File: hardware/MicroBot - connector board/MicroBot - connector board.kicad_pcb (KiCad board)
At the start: 2 copper layers, 88.9 x 76.8 mm, 36 parts, among them J0 SMM_Mega_Shield_Connector, J1 X_Axis_Stepper_Controller, J2 Y_Axis_Stepper_Controller, J3 gen4-IB, J4 24VDC, M1 Motor_DC, U1 L9110_H-Bridge, U2 R-78C12-1.0, U3 R-78C12-1.0, U5 OKI-78SR-5_1.5-W36-C

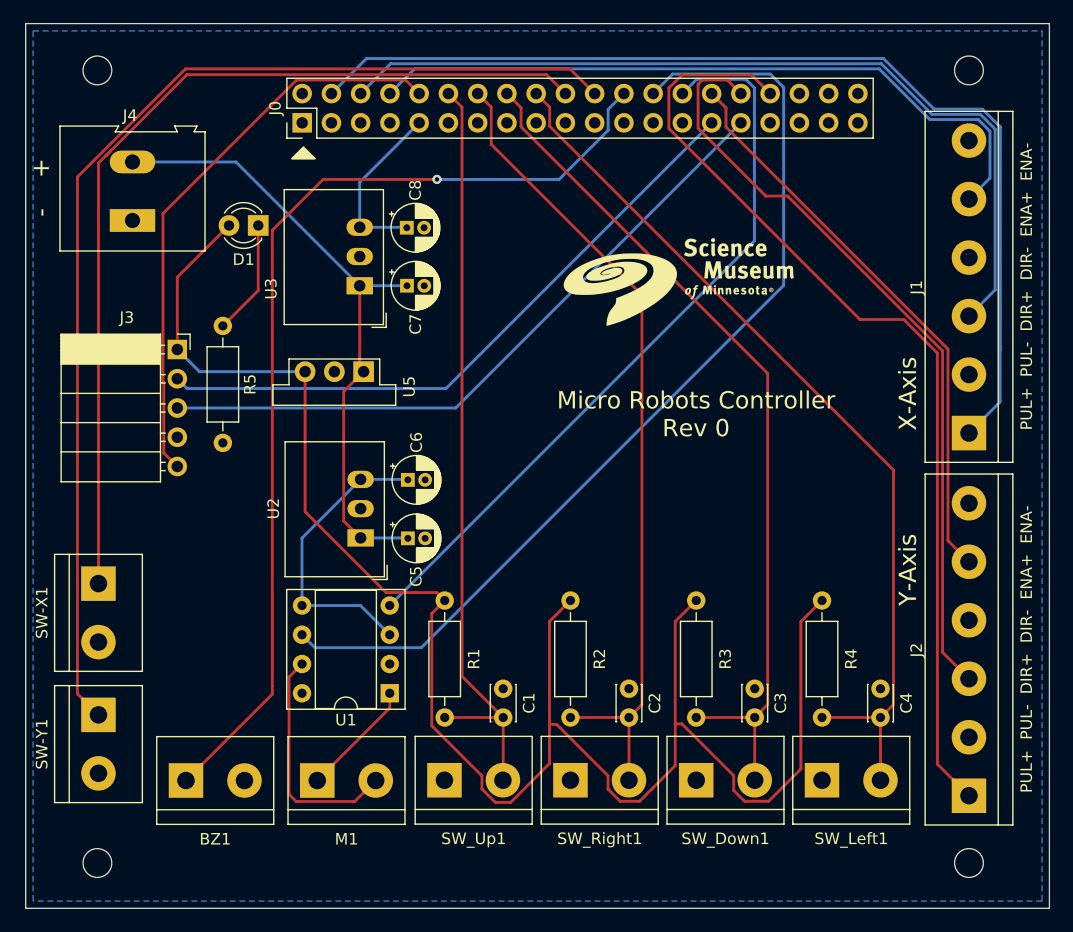
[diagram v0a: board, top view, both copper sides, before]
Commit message: fix error in PCB layout
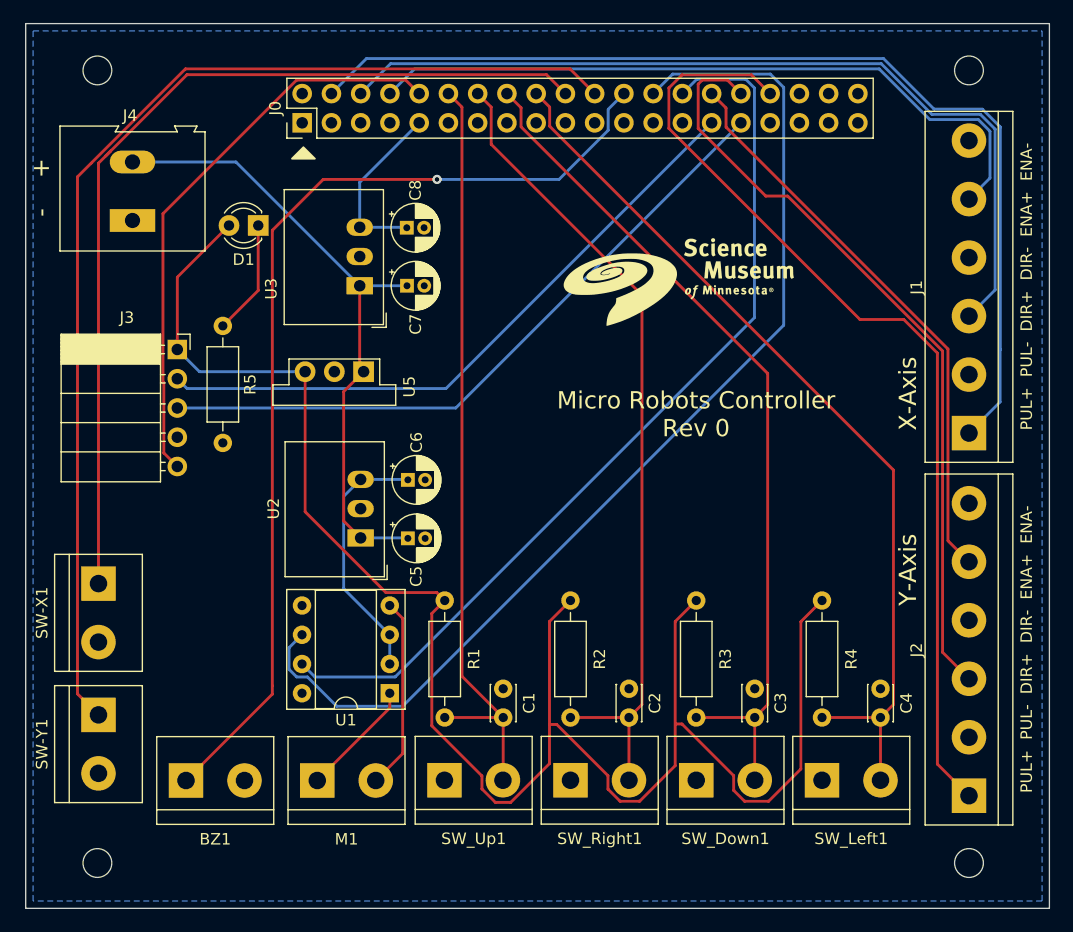
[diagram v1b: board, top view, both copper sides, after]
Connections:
- U1 pad 2: GND -> Net-(C6-Pad1)
- U1 pad 4: /MotorB -> Net-(M1-Pad2)
- U1 pad 5: Net-(C6-Pad1) -> GND
- U1 pad 7: Net-(M1-Pad2) -> /MotorB
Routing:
- net /MotorB: track 65.1 -> 79.7 mm
- net /MotorA: track 85.0 -> 94.6 mm
- net Net-(M1-Pad2): track 20.3 -> 16.6 mm
- net Net-(C6-Pad1): track 25.9 -> 22.4 mm
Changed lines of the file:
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@@
       (net 42 "Net-(M1-Pad1)") (pinfunction "OA") (pintype "output"))
     (pad "2" thru_hole oval (at 0 2.54 180) (size 1.6 1.6) (drill 0.8) (layers *.Cu *.Mask)
-      (net 2 "GND") (pinfunction "GND") (pintype "power_in"))
+      (net 3 "Net-(C6-Pad1)") (pinfunction "VCC") (pintype "power_in"))
     (pad "3" thru_hole oval (at 0 5.08 180) (size 1.6 1.6) (drill 0.8) (layers *.Cu *.Mask)
       (net 3 "Net-(C6-Pad1)") (pinfunction "VCC") (pintype "power_in"))
     (pad "4" thru_hole oval (at 0 7.62 180) (size 1.6 1.6) (drill 0.8) (layers *.Cu *.Mask)
-      (net 28 "/MotorB") (pinfunction "IB") (pintype "input"))
+      (net 43 "Net-(M1-Pad2)") (pinfunction "OB") (pintype "output"))
     (pad "5" thru_hole oval (at 7.62 7.62 180) (size 1.6 1.6) (drill 0.8) (layers *.Cu *.Mask)
-      (net 3 "Net-(C6-Pad1)") (pinfunction "VCC") (pintype "power_in"))
+      (net 2 "GND") (pinfunction "GND") (pintype "power_in"))
     (pad "6" thru_hole oval (at 7.62 5.08 180) (size 1.6 1.6) (drill 0.8) (layers *.Cu *.Mask)
       (net 26 "/MotorA") (pinfunction "IA") (pintype "input"))
     (pad "7" thru_hole oval (at 7.62 2.54 180) (size 1.6 1.6) (drill 0.8) (layers *.Cu *.Mask)
-      (net 43 "Net-(M1-Pad2)") (pinfunction "OB") (pintype "output"))
+      (net 28 "/MotorB") (pinfunction "IB") (pintype "input"))
     (pad "8" thru_hole oval (at 7.62 0 180) (size 1.6 1.6) (drill 0.8) (layers *.Cu *.Mask)
       (net 2 "GND") (pinfunction "GND") (pintype "power_in"))
@@
   (segment (start 147.5655 71.1345) (end 143.3 75.4) (width 0.25) (layer "B.Cu") (net 1))
   (segment (start 143.3 75.4) (end 132.7 75.4) (width 0.25) (layer "B.Cu") (net 1))
-  (segment (start 120.975989 106.542088) (end 120.975989 112.403489) (width 0.25) (layer "B.Cu") (net 3))
-  (segment (start 126.055989 112.403489) (end 128.595989 114.943489) (width 0.25) (layer "B.Cu") (net 3))
+  (segment (start 124.591478 110.938978) (end 128.595989 114.943489) (width 0.25) (layer "B.Cu") (net 3))
+  (segment (start 126.065989 101.452088) (end 124.591478 102.926599) (width 0.25) (layer "B.Cu") (net 3))
+  (segment (start 124.591478 102.926599) (end 124.591478 110.938978) (width 0.25) (layer "B.Cu") (net 3))
   (segment (start 130.129989 101.452088) (end 130.16939 101.491489) (width 0.25) (layer "B.Cu") (net 3))
-  (segment (start 120.975989 112.403489) (end 126.055989 112.403489) (width 0.25) (layer "B.Cu") (net 3))
+  (segment (start 128.595989 114.943489) (end 128.595989 117.483489) (width 0.25) (layer "B.Cu") (net 3))
   (segment (start 126.065989 101.452088) (end 130.129989 101.452088) (width 0.25) (layer "B.Cu") (net 3))
-  (segment (start 126.065989 101.452088) (end 120.975989 106.542088) (width 0.25) (layer "B.Cu") (net 3))
   (segment (start 125.987489 79.554489) (end 125.987489 75.6485) (width 0.25) (layer "B.Cu") (net 4))
   (segment (start 125.987489 79.554489) (end 130.036088 79.554489) (width 0.25) (layer "B.Cu") (net 4))
@@
   (segment (start 102.67713 73.97713) (end 110.85426 65.8) (width 0.25) (layer "F.Cu") (net 23))
   (segment (start 144.245989 65.8) (end 146.390989 67.945) (width 0.25) (layer "F.Cu") (net 23))
-  (segment (start 153.165509 66.25048) (end 151.470989 67.945) (width 0.25) (layer "B.Cu") (net 26))
-  (segment (start 131.332 116.068) (end 162.8055 84.5945) (width 0.25) (layer "B.Cu") (net 26))
-  (segment (start 122.1005 116.068) (end 131.332 116.068) (width 0.25) (layer "B.Cu") (net 26))
-  (segment (start 120.975989 114.943489) (end 122.1005 116.068) (width 0.25) (layer "B.Cu") (net 26))
-  (segment (start 161.65048 66.25048) (end 153.165509 66.25048) (width 0.25) (layer "B.Cu") (net 26))
-  (segment (start 162.8055 84.5945) (end 162.8055 67.4055) (width 0.25) (layer "B.Cu") (net 26))
-  (segment (start 162.8055 67.4055) (end 161.65048 66.25048) (width 0.25) (layer "B.Cu") (net 26))
-  (segment (start 159.506999 66.7) (end 155.255989 66.7) (width 0.25) (layer "B.Cu") (net 28))
-  (segment (start 160.2655 80.733978) (end 160.2655 67.458501) (width 0.25) (layer "B.Cu") (net 28))
-  (segment (start 128.595989 112.403489) (end 160.2655 80.733978) (width 0.25) (layer "B.Cu") (net 28))
-  (segment (start 155.255989 66.7) (end 154.010989 67.945) (width 0.25) (layer "B.Cu") (net 28))
-  (segment (start 160.2655 67.458501) (end 159.506999 66.7) (width 0.25) (layer "B.Cu") (net 28))
+  (segment (start 119.851478 117.949278) (end 119.851478 116.068) (width 0.25) (layer "B.Cu") (net 26))
+  (segment (start 161.65048 66.25048) (end 162.8055 67.4055) (width 0.25) (layer "B.Cu") (net 26))
+  (segment (start 151.470989 67.945) (end 153.165509 66.25048) (width 0.25) (layer "B.Cu") (net 26))
+  (segment (start 153.165509 66.25048) (end 161.65048 66.25048) (width 0.25) (layer "B.Cu") (net 26))
+  (segment (start 129.7205 121.148) (end 123.981778 121.148) (width 0.25) (layer "B.Cu") (net 26))
+  (segment (start 162.8055 88.063) (end 129.7205 121.148) (width 0.25) (layer "B.Cu") (net 26))
+  (segment (start 162.8055 67.4055) (end 162.8055 88.063) (width 0.25) (layer "B.Cu") (net 26))
+  (segment (start 123.981778 121.148) (end 121.441778 118.608) (width 0.25) (layer "B.Cu") (net 26))
+  (segment (start 119.851478 116.068) (end 120.975989 114.943489) (width 0.25) (layer "B.Cu") (net 26))
+  (segment (start 121.441778 118.608) (end 120.5102 118.608) (width 0.25) (layer "B.Cu") (net 26))
+  (segment (start 120.5102 118.608) (end 119.851478 117.949278) (width 0.25) (layer "B.Cu") (net 26))
+  (segment (start 154.010989 67.945) (end 155.255989 66.7) (width 0.25) (layer "B.Cu") (net 28))
+  (segment (start 129.061778 118.608) (end 122.1005 118.608) (width 0.25) (layer "B.Cu") (net 28))
+  (segment (start 159.506999 66.7) (end 160.2655 67.458501) (width 0.25) (layer "B.Cu") (net 28))
+  (segment (start 160.2655 87.404278) (end 129.061778 118.608) (width 0.25) (layer "B.Cu") (net 28))
+  (segment (start 160.2655 67.458501) (end 160.2655 87.404278) (width 0.25) (layer "B.Cu") (net 28))
+  (segment (start 122.1005 118.608) (end 120.975989 117.483489) (width 0.25) (layer "B.Cu") (net 28))
+  (segment (start 155.255989 66.7) (end 159.506999 66.7) (width 0.25) (layer "B.Cu") (net 28))
   (segment (start 133.475989 93.56) (end 156.550989 70.485) (width 0.25) (layer "B.Cu") (net 29))
   (segment (start 110.995989 93.56) (end 133.475989 93.56) (width 0.25) (layer "B.Cu") (net 29))
@@
   (segment (start 122.3 127.6) (end 128.595989 121.304011) (width 0.25) (layer "F.Cu") (net 42))
   (segment (start 128.595989 121.304011) (end 128.595989 120.023489) (width 0.25) (layer "F.Cu") (net 42))
-  (segment (start 125.555489 129.424511) (end 120.475489 129.424511) (width 0.25) (layer "F.Cu") (net 43))
-  (segment (start 119.851478 128.8005) (end 119.851478 118.608) (width 0.25) (layer "F.Cu") (net 43))
-  (segment (start 127.38 127.6) (end 125.555489 129.424511) (width 0.25) (layer "F.Cu") (net 43))
-  (segment (start 119.851478 118.608) (end 120.975989 117.483489) (width 0.25) (layer "F.Cu") (net 43))
-  (segment (start 120.475489 129.424511) (end 119.851478 128.8005) (width 0.25) (layer "F.Cu") (net 43))
+  (segment (start 127.38 127.6) (end 129.7205 125.2595) (width 0.25) (layer "F.Cu") (net 43))
+  (segment (start 129.7205 113.528) (end 128.595989 112.403489) (width 0.25) (layer "F.Cu") (net 43))
+  (segment (start 129.7205 125.2595) (end 129.7205 113.528) (width 0.25) (layer "F.Cu") (net 43))
   (segment (start 126.324989 92.094489) (end 124.591469 93.828009) (width 0.25) (layer "F.Cu") (net 44))
   (segment (start 124.591469 93.828009) (end 124.591469 105.057568) (width 0.25) (layer "F.Cu") (net 44))
